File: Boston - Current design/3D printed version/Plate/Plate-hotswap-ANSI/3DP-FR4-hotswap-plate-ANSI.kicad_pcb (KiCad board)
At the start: 2 copper layers, 396 x 161 mm, 41 parts

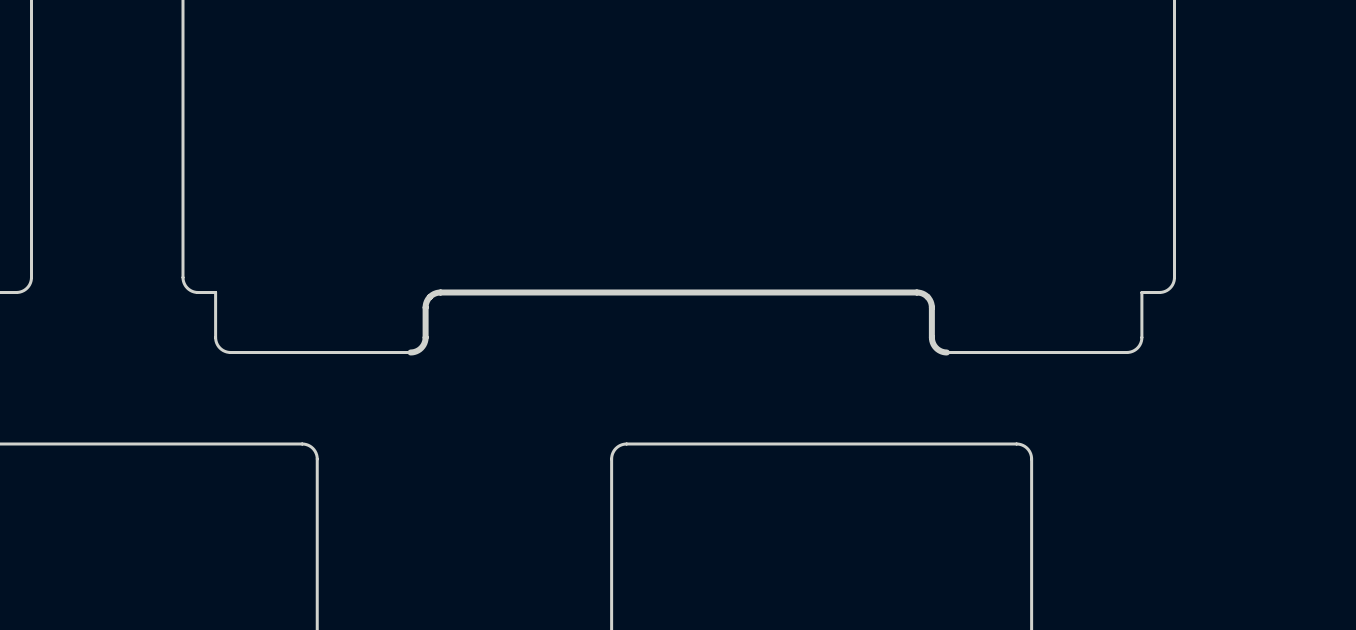
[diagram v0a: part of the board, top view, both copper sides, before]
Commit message: Fixed some other sharp corners
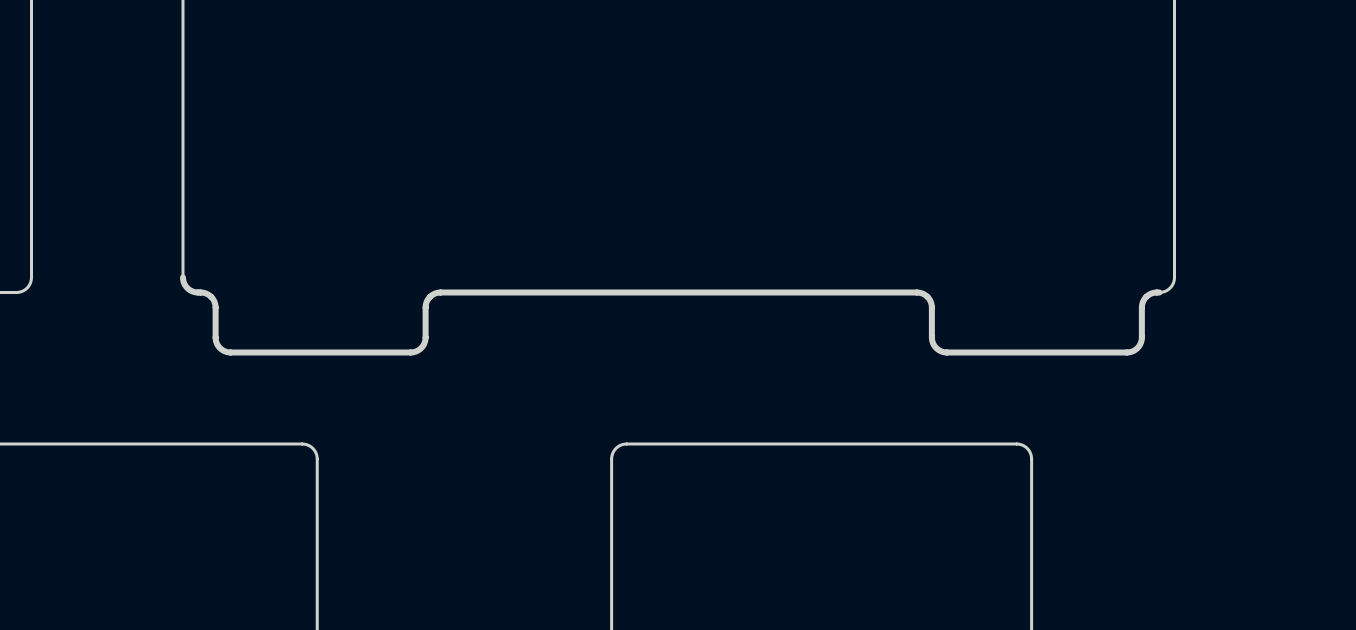
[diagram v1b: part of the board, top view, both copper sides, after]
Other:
- outline, holes or cut-outs redrawn
- board text added: "Hotswap plate - ANSI June 27, 2023"
- board text removed: "Hotswap plate - ANSI Mar 26, 2023"
